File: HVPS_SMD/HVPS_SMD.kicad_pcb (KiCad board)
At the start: 2 copper layers, 36.8 x 22.9 mm, 22 parts, among them J1 CONN_01X02, J2 CONN_01X02, J3 CONN_01X02, Q1 AO4294, T1 WE-FLEX_ER11_5, U1 LM3478SOIC8

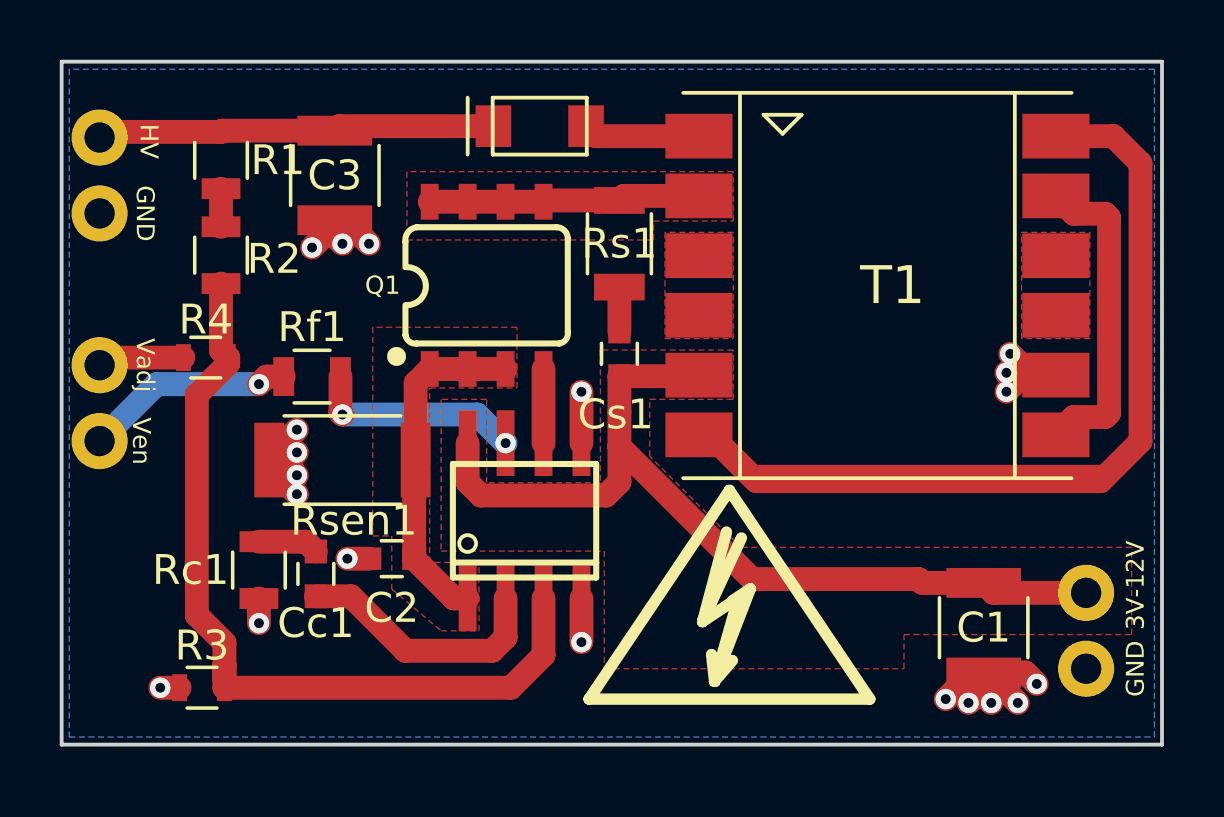
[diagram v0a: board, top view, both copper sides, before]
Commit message: Fixed external footprint references
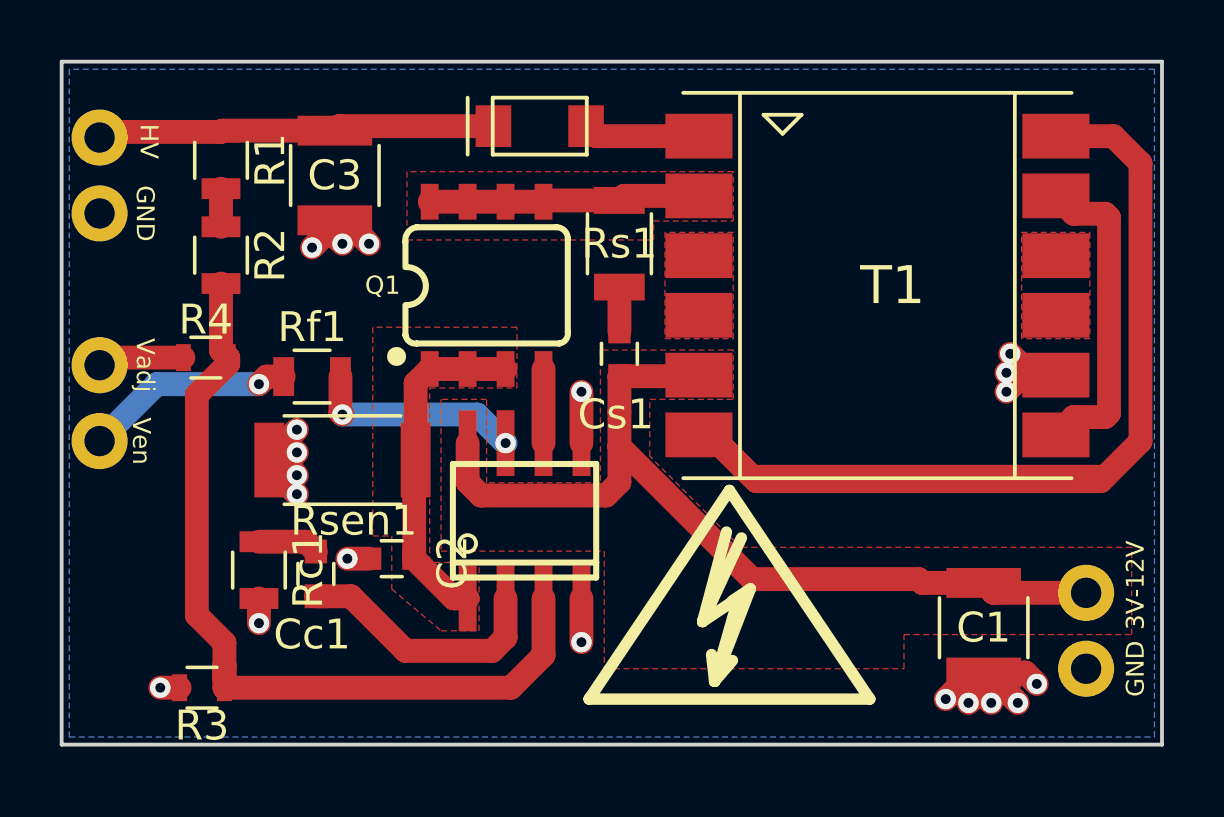
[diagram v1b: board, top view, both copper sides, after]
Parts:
- C1, C3: footprint Capacitors_SMD:C_1210 -> lib_fp:C_1210
- C2, Cc1, Cs1: footprint Capacitors_SMD:C_0603 -> lib_fp:C_0603
- D1: footprint nixiemisc:nixiemisc-DO-219AB -> lib_fp:nixiemisc-DO-219AB
- J1, J2, J3: footprint SparkFun-Connectors:SparkFun-Connectors-1X02_NO_SILK -> lib_fp:SparkFun-Connectors-1X02_NO_SILK
- Q1: footprint nixiemisc:nixiemisc-SO08 -> lib_fp:nixiemisc-SO08
- R1, R2, Rc1, Rf1: footprint Resistors_SMD:R_0805 -> lib_fp:R_0805
- R3, R4: footprint Resistors_SMD:R_0603 -> lib_fp:R_0603
- Rs1: footprint Resistors_SMD:R_1206 -> lib_fp:R_1206
- Rsen1: footprint Resistors_SMD:R_2010 -> lib_fp:R_2010
- T1: footprint nixiemisc:nixiemisc-WE-FLEX_ER11_5 -> lib_fp:nixiemisc-WE-FLEX_ER11_5
- U1: footprint nixiemisc:nixiemisc-SOIC8 -> lib_fp:nixiemisc-SOIC8
